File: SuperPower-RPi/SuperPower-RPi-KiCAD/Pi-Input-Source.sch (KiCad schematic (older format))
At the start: 12 parts, among them J3 Screw_Terminal_01x02, P1 USB_C_Plug_USB2.0, Q3 Q_PMOS_GSD, Q6 Q_PMOS_GSD, Q7 Q_PMOS_GSD

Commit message: Component Updates.
Redid battery reverse polarty circuit to use an NMOS.

Added note for important parameters in overvoltage protection circuit.

(cherry picked from commit 69b0d79b222f07f7c875c3ca5cc6bb34230cf411)
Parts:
- removed Q6: Q_PMOS_GSD, symbol Device:Q_PMOS_GSD
- added Q?: Q_PMOS_GSD, symbol Device:Q_PMOS_GSD
- D3: footprint (none) -> Diode_SMD:D_SOD-123
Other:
- note added: "Vz(D4) + Vgs(th)(Q2) is critical for overvoltage threshold."
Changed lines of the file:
@@
 Text HLabel 9550 3000 2    50   Output ~ 0
 Vout
-Text Notes 4850 5850 0    50   ~ 0
+Text Notes 2450 5900 0    50   ~ 0
 NOTE:\nProbably USB-C and screw-terminals for solar.  \nMicroUSB possible.
 Text Notes 4150 2150 0    50   ~ 0
@@
 F 0 "D3" V 4804 3320 50  0000 L CNN
 F 1 "D_Zener_Small" V 4895 3320 50  0000 L CNN
-F 2 "" V 4850 3250 50  0001 C CNN
+F 2 "Diode_SMD:D_SOD-123" V 4850 3250 50  0001 C CNN
 F 3 "~" V 4850 3250 50  0001 C CNN
 	1    4850 3250
@@
 $EndComp
 $Comp
-L Device:Q_PMOS_GSD Q6
-U 1 1 5FA8CB6D
-P 7900 3550
-F 0 "Q6" H 7750 3600 50  0000 C CNN
-F 1 "Q_PMOS_GSD" V 8150 3650 50  0000 C CNN
-F 2 "" H 8100 3650 50  0001 C CNN
-F 3 "~" H 7900 3550 50  0001 C CNN
-	1    7900 3550
-	1    0    0    -1
-$EndComp
-$Comp
 L Device:R_Small R18
 U 1 1 5FA8D2AB
@@
 Text Notes 6950 4500 0    50   ~ 0
 Overvoltage Protection
+Text Notes 6450 4850 0    50   ~ 0
+Vz(D4) + Vgs(th)(Q2) is critical for overvoltage threshold.
+$Comp
+L Device:Q_PMOS_GSD Q?
+U 1 1 5FA8A6C8
+P 7900 3550
+F 0 "Q?" V 8242 3550 50  0000 C CNN
+F 1 "Q_PMOS_GSD" V 8151 3550 50  0000 C CNN
+F 2 "" H 8100 3650 50  0001 C CNN
+F 3 "~" H 7900 3550 50  0001 C CNN
+	1    7900 3550
+	1    0    0    1
+$EndComp
 $EndSCHEMATC

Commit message: Updated USB connector and it's meta-data.
(cherry picked from commit f942f8875393aea1f502e9979f1017d3426d4be4)
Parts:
- removed P1: USB_C_Plug_USB2.0, symbol Connector:USB_C_Plug_USB2.0
- added J?: USB_C_Receptacle_USB2.0, Connector_USB:USB_C_Receptacle_HRO_TYPE-C-31-M-12, symbol Connector:USB_C_Receptacle_USB2.0
- D3: footprint Diode_SMD:D_SOD-123 -> (none)
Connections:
- wire segments 43 -> 49
- no-connect marks 2 -> 4
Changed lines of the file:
@@
 NoConn ~ 3050 3300
-$Comp
-L Connector:USB_C_Plug_USB2.0 P1
-U 1 1 5FA09B52
-P 2450 3600
-F 0 "P1" H 2557 4467 50  0000 C CNN
-F 1 "USB_C_Plug_USB2.0" H 2557 4376 50  0000 C CNN
-F 2 "" H 2600 3600 50  0001 C CNN
-F 3 "https://www.usb.org/sites/default/files/documents/usb_type-c.zip" H 2600 3600 50  0001 C CNN
-	1    2450 3600
-	1    0    0    -1
-$EndComp
 $Comp
 L power:PWR_FLAG #FLG0106
@@
 $EndComp
 Wire Wire Line
-	3050 3700 3300 3700
-Wire Wire Line
-	3300 3500 3050 3500
+	3050 3700 3150 3700
+Wire Wire Line
+	3300 3500 3150 3500
 Text HLabel 3300 3500 2    50   Output ~ 0
 D-
@@
 F 0 "D3" V 4804 3320 50  0000 L CNN
 F 1 "D_Zener_Small" V 4895 3320 50  0000 L CNN
-F 2 "Diode_SMD:D_SOD-123" V 4850 3250 50  0001 C CNN
+F 2 "" V 4850 3250 50  0001 C CNN
 F 3 "~" V 4850 3250 50  0001 C CNN
 	1    4850 3250
@@
 	1    0    0    1
 $EndComp
+$Comp
+L Connector:USB_C_Receptacle_USB2.0 J?
+U 1 1 5FA11947
+P 2450 3600
+F 0 "J?" H 2557 4467 50  0000 C CNN
+F 1 "USB_C_Receptacle_USB2.0" H 2557 4376 50  0000 C CNN
+F 2 "Connector_USB:USB_C_Receptacle_HRO_TYPE-C-31-M-12" H 2600 3600 50  0001 C CNN
+F 3 "https://datasheet.lcsc.com/szlcsc/1811131825_Korean-Hroparts-Elec-TYPE-C-31-M-12_C165948.pdf" H 2600 3600 50  0001 C CNN
+F 4 "Korean Hroparts Elec" H 2450 3600 50  0001 C CNN "Mfg"
+F 5 "TYPE-C-31-M-12" H 2450 3600 50  0001 C CNN "Mfg PN"
+	1    2450 3600
+	1    0    0    -1
+$EndComp
+Wire Wire Line
+	3050 3600 3150 3600
+Wire Wire Line
+	3150 3600 3150 3500
+Connection ~ 3150 3500
+Wire Wire Line
+	3150 3500 3050 3500
+Wire Wire Line
+	3050 3800 3150 3800
+Wire Wire Line
+	3150 3800 3150 3700
+Connection ~ 3150 3700
+Wire Wire Line
+	3150 3700 3300 3700
+NoConn ~ 3050 4200
+NoConn ~ 3050 4100
 $EndSCHEMATC

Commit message: Part Meta-data updates continued.
(cherry picked from commit d0ad2c93dfb1e315a7dc98683a53ed7dcb5f49ff)
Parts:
- gave numbers to parts that had none: 2
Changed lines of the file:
@@
 Vz(D4) + Vgs(th)(Q2) is critical for overvoltage threshold.
 $Comp
-L Device:Q_PMOS_GSD Q?
+L Device:Q_PMOS_GSD Q2
 U 1 1 5FA8A6C8
 P 7900 3550
-F 0 "Q?" V 8242 3550 50  0000 C CNN
+F 0 "Q2" V 8242 3550 50  0000 C CNN
 F 1 "Q_PMOS_GSD" V 8151 3550 50  0000 C CNN
 F 2 "" H 8100 3650 50  0001 C CNN
@@
 $EndComp
 $Comp
-L Connector:USB_C_Receptacle_USB2.0 J?
+L Connector:USB_C_Receptacle_USB2.0 J6
 U 1 1 5FA11947
 P 2450 3600
-F 0 "J?" H 2557 4467 50  0000 C CNN
+F 0 "J6" H 2557 4467 50  0000 C CNN
 F 1 "USB_C_Receptacle_USB2.0" H 2557 4376 50  0000 C CNN
 F 2 "Connector_USB:USB_C_Receptacle_HRO_TYPE-C-31-M-12" H 2600 3600 50  0001 C CNN

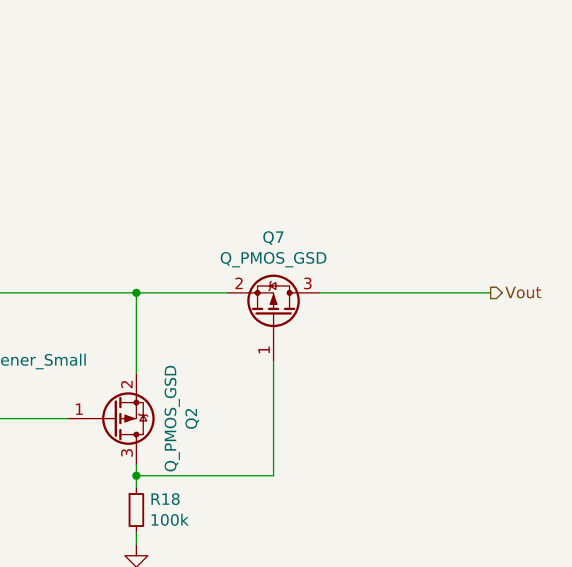
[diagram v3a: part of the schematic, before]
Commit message: Added local footprint library, and associated components.
(cherry picked from commit 78b1abfd5fe55b90039e798d35239acda24b0417)
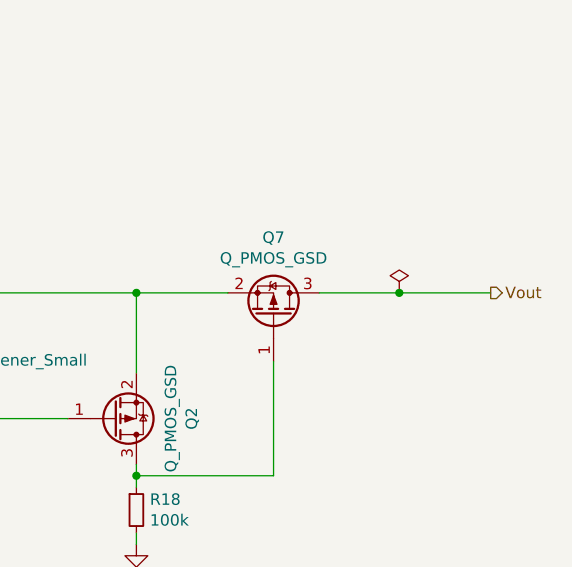
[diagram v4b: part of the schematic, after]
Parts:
- D3, D4, D5: footprint (none) -> Diode_SMD:D_SOD-123
- Q2, Q3, Q7: footprint (none) -> Package_TO_SOT_SMD:SOT-23; Mfg (none) -> FIX FOOTPRINT
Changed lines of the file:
@@
 F 0 "Q3" V 4892 3100 50  0000 C CNN
 F 1 "Q_PMOS_GSD" V 4801 3100 50  0000 C CNN
-F 2 "" H 4750 3200 50  0001 C CNN
+F 2 "Package_TO_SOT_SMD:SOT-23" H 4750 3200 50  0001 C CNN
 F 3 "~" H 4550 3100 50  0001 C CNN
+F 4 "FIX FOOTPRINT" H 4550 3100 50  0001 C CNN "Mfg"
 	1    4550 3100
 	0    -1   -1   0
@@
 F 0 "D3" V 4804 3320 50  0000 L CNN
 F 1 "D_Zener_Small" V 4895 3320 50  0000 L CNN
-F 2 "" V 4850 3250 50  0001 C CNN
+F 2 "Diode_SMD:D_SOD-123" V 4850 3250 50  0001 C CNN
 F 3 "~" V 4850 3250 50  0001 C CNN
 	1    4850 3250
@@
 F 0 "D4" V 6454 3820 50  0000 L CNN
 F 1 "D_Zener_Small" V 6545 3820 50  0000 L CNN
-F 2 "" V 6500 3750 50  0001 C CNN
+F 2 "Diode_SMD:D_SOD-123" V 6500 3750 50  0001 C CNN
 F 3 "~" V 6500 3750 50  0001 C CNN
 	1    6500 3750
@@
 F 0 "D5" V 7154 3320 50  0000 L CNN
 F 1 "D_Zener_Small" V 7245 3320 50  0000 L CNN
-F 2 "" V 7200 3250 50  0001 C CNN
+F 2 "Diode_SMD:D_SOD-123" V 7200 3250 50  0001 C CNN
 F 3 "~" V 7200 3250 50  0001 C CNN
 	1    7200 3250
@@
 F 0 "Q7" V 8942 3100 50  0000 C CNN
 F 1 "Q_PMOS_GSD" V 8851 3100 50  0000 C CNN
-F 2 "" H 8800 3200 50  0001 C CNN
+F 2 "Package_TO_SOT_SMD:SOT-23" H 8800 3200 50  0001 C CNN
 F 3 "~" H 8600 3100 50  0001 C CNN
+F 4 "FIX FOOTPRINT" H 8600 3100 50  0001 C CNN "Mfg"
 	1    8600 3100
 	0    1    -1   0
@@
 	8000 3800 8000 3750
 Wire Wire Line
-	9550 3000 8800 3000
+	9550 3000 9150 3000
 Wire Wire Line
 	3450 3000 4150 3000
@@
 F 0 "Q2" V 8242 3550 50  0000 C CNN
 F 1 "Q_PMOS_GSD" V 8151 3550 50  0000 C CNN
-F 2 "" H 8100 3650 50  0001 C CNN
+F 2 "Package_TO_SOT_SMD:SOT-23" H 8100 3650 50  0001 C CNN
 F 3 "~" H 7900 3550 50  0001 C CNN
+F 4 "FIX FOOTPRINT" H 7900 3550 50  0001 C CNN "Mfg"
 	1    7900 3550
 	1    0    0    1
@@
 NoConn ~ 3050 4200
 NoConn ~ 3050 4100
+$Comp
+L power:PWR_FLAG #FLG0109
+U 1 1 5FBA187F
+P 9150 3000
+F 0 "#FLG0109" H 9150 3075 50  0001 C CNN
+F 1 "PWR_FLAG" V 9150 3128 50  0001 L CNN
+F 2 "" H 9150 3000 50  0001 C CNN
+F 3 "~" H 9150 3000 50  0001 C CNN
+	1    9150 3000
+	1    0    0    -1
+$EndComp
+Connection ~ 9150 3000
+Wire Wire Line
+	9150 3000 8800 3000
 $EndSCHEMATC

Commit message: Added temporary footprints and imported into pcb.
(cherry picked from commit a685dfc635e321a03e1c1fd194e70e2193ef2183)
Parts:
- D3, D4, D5: Mfg (none) -> FIX FOOTPRINT
- J3: footprint (none) -> Connector_Phoenix_MC:PhoenixContact_MCV_1,5_2-GF-3.5_1x02_P3.50mm_Vertical_ThreadedFlange_MountHole; Mfg (none) -> FIX FOOTPRINT
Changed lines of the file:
@@
 F 0 "J3" H 2318 1525 50  0000 C CNN
 F 1 "Screw_Terminal_01x02" H 2318 1616 50  0000 C CNN
-F 2 "" H 2400 1850 50  0001 C CNN
+F 2 "Connector_Phoenix_MC:PhoenixContact_MCV_1,5_2-GF-3.5_1x02_P3.50mm_Vertical_ThreadedFlange_MountHole" H 2400 1850 50  0001 C CNN
 F 3 "~" H 2400 1850 50  0001 C CNN
+F 4 "FIX FOOTPRINT" H 2400 1850 50  0001 C CNN "Mfg"
 	1    2400 1850
 	-1   0    0    1
@@
 F 2 "Diode_SMD:D_SOD-123" V 4850 3250 50  0001 C CNN
 F 3 "~" V 4850 3250 50  0001 C CNN
+F 4 "FIX FOOTPRINT" H 4850 3250 50  0001 C CNN "Mfg"
 	1    4850 3250
 	0    1    1    0
@@
 F 2 "Diode_SMD:D_SOD-123" V 6500 3750 50  0001 C CNN
 F 3 "~" V 6500 3750 50  0001 C CNN
+F 4 "FIX FOOTPRINT" H 6500 3750 50  0001 C CNN "Mfg"
 	1    6500 3750
 	0    1    1    0
@@
 F 2 "Diode_SMD:D_SOD-123" V 7200 3250 50  0001 C CNN
 F 3 "~" V 7200 3250 50  0001 C CNN
+F 4 "FIX FOOTPRINT" H 7200 3250 50  0001 C CNN "Mfg"
 	1    7200 3250
 	0    1    1    0

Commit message: Updated components based on 2020/11/08 team meeting.
(cherry picked from commit e5b001aa9b91e1123a0a2394fa23acf6ac376265)
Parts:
- J3: footprint Connector_Phoenix_MC:PhoenixContact_MCV_1,5_2-GF-3.5_1x02_P3.50mm_Vertical_ThreadedFlange_MountHole -> TerminalBlock_4Ucon:TerminalBlock_4Ucon_1x02_P3.50mm_Horizontal; Mfg FIX FOOTPRINT -> Adafruit; Mfg PN (none) -> 724
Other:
- note added: "NOTE:\nscrew-terminals for solar."
- note added: "https://www.adafruit.com/product/724"
- note removed: "NOTE:\nProbably USB-C and screw-terminals for solar. \nMicroUSB possible."
- note removed: "Should the USB VBUS be moved to after the input protection?"
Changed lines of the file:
@@
 F 0 "J3" H 2318 1525 50  0000 C CNN
 F 1 "Screw_Terminal_01x02" H 2318 1616 50  0000 C CNN
-F 2 "Connector_Phoenix_MC:PhoenixContact_MCV_1,5_2-GF-3.5_1x02_P3.50mm_Vertical_ThreadedFlange_MountHole" H 2400 1850 50  0001 C CNN
-F 3 "~" H 2400 1850 50  0001 C CNN
-F 4 "FIX FOOTPRINT" H 2400 1850 50  0001 C CNN "Mfg"
+F 2 "TerminalBlock_4Ucon:TerminalBlock_4Ucon_1x02_P3.50mm_Horizontal" H 2400 1850 50  0001 C CNN
+F 3 "https://www.adafruit.com/product/724" H 2400 1850 50  0001 C CNN
+F 4 "Adafruit" H 2400 1850 50  0001 C CNN "Mfg"
+F 5 "724" H 2400 1850 50  0001 C CNN "Mfg PN"
 	1    2400 1850
 	-1   0    0    1
@@
 Vout
 Text Notes 2450 5900 0    50   ~ 0
-NOTE:\nProbably USB-C and screw-terminals for solar.  \nMicroUSB possible.
-Text Notes 4150 2150 0    50   ~ 0
-Should the USB VBUS be moved to after the input protection?
+NOTE:\nscrew-terminals for solar.
 $Comp
 L Device:D_Zener_Small D3
@@
 Wire Wire Line
 	9150 3000 8800 3000
+Text Notes 1950 1400 0    50   ~ 0
+https://www.adafruit.com/product/724
 $EndSCHEMATC

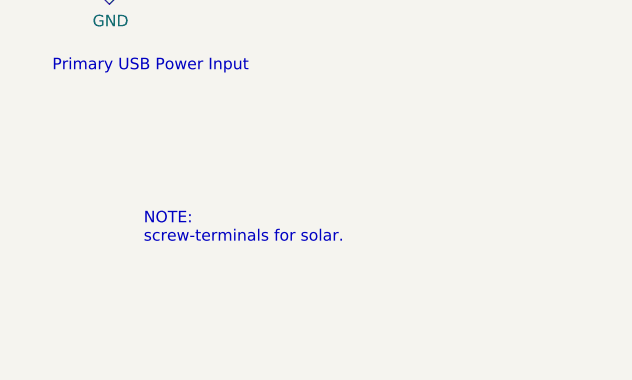
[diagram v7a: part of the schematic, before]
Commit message: Changed Boost Converter passives to the values included in the eval kit.
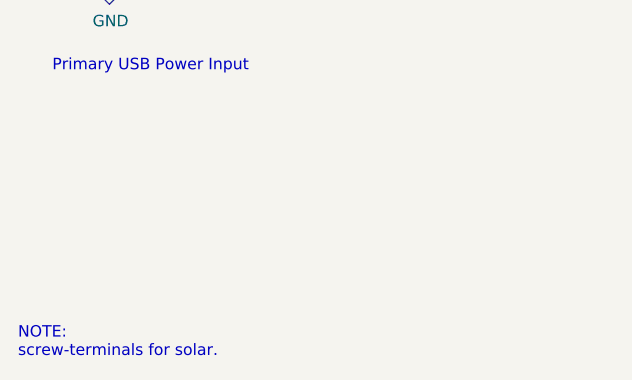
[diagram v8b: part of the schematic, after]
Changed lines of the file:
@@
 Text HLabel 9550 3000 2    50   Output ~ 0
 Vout
-Text Notes 2450 5900 0    50   ~ 0
+Text Notes 1900 6400 0    50   ~ 0
 NOTE:\nscrew-terminals for solar.
 $Comp
